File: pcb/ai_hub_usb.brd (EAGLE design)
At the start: 82.5 x 38.1 mm, 31 parts, among them IC1 FE1.1S

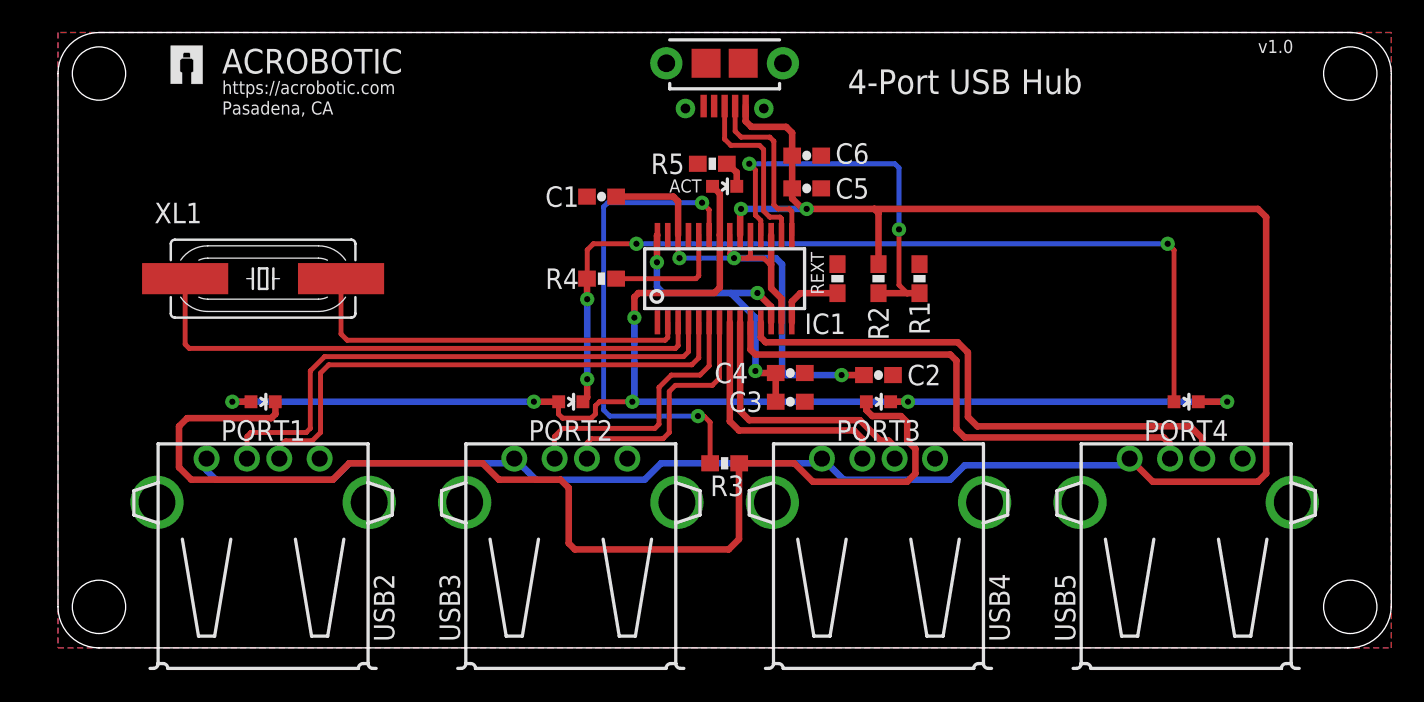
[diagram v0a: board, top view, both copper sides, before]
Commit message: redesign: gang power control, smaller layout
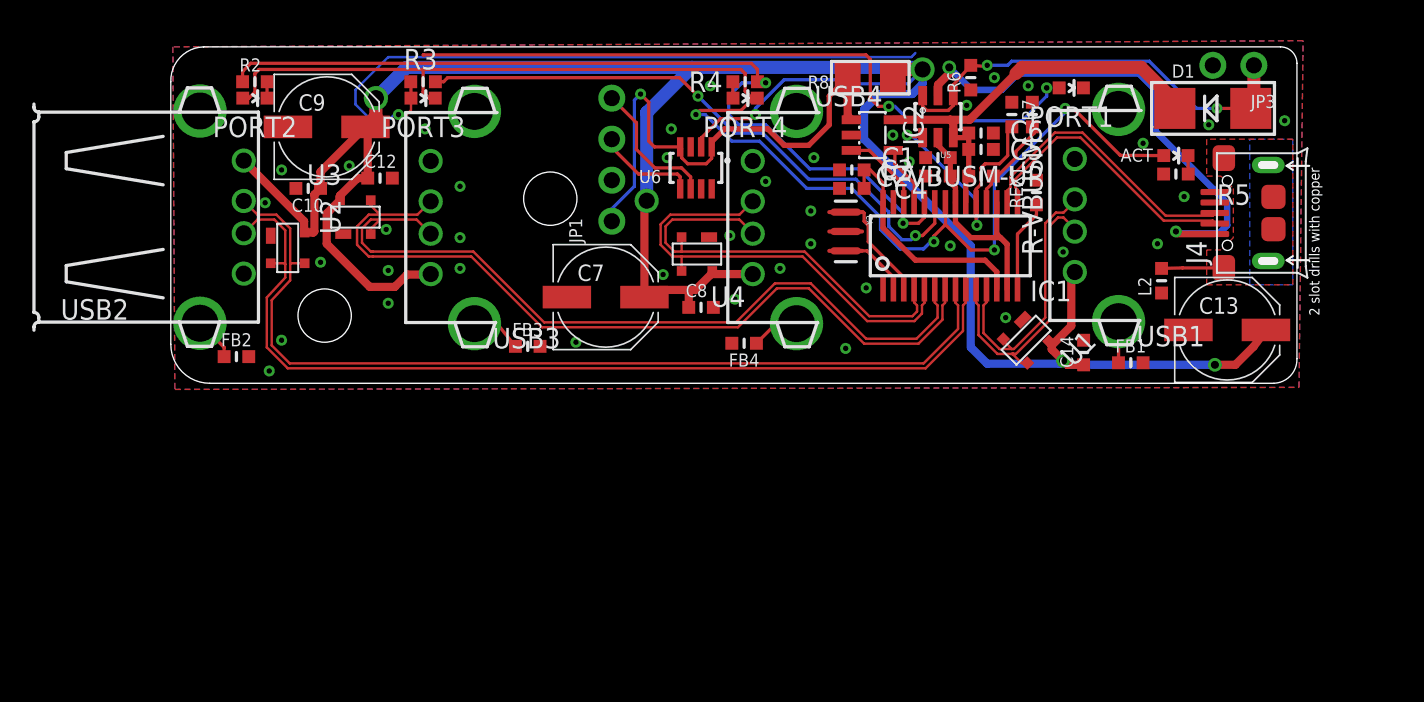
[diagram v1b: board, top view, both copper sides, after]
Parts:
- removed FRAME1: FRAME-LETTER, Ai_Miscellany:CREATIVE-COMMONS
- removed R1: 100K, Ai_Passives:RES-0603
- removed STANDOFF2, STANDOFF3: STAND-OFF4, Ai_Electromechanical:STAND-OFF-4
- removed U$5, U$6: AI-LOGOXS, Ai_Miscellany:AI-LOGO-XS
- removed USB5: USBA-PTH, Ai_Connectors:USB-A-F-PTH
- removed XL1: 12MHz, Ai_FrequencyControl:HC49UP
- added C10, C12, C14, C8: 0.1uF, microbuilder:_0603MP
- added C13, C7, C9: (no value), SparkFun-Passives:PANASONIC_D
- added D1: (no value), microbuilder:SMADIODE
- added FB1, FB2, FB3, FB4, L2: (no value), microbuilder:_0603MP
- added IC2: TPS2041BDBV, tps204xb_205xb:SOT23-5L
- added J4: MICRO-B-SMD_340005001, connectors:MICRO-USB
- added JP1: (no value), microbuilder:1X04_ROUND
- added JP3: (no value), microbuilder:1X02_ROUND
- added R-VBUSM, R6, R7: 100K, microbuilder:_0603MP
- added R-VBUSM-UP: 47K, microbuilder:_0603MP
- added R8: (no value), microbuilder:1206
- added U1, U2, U3, U4: PRTR5V0U2X, esd:SOT-143B
- added U5: IRF5810TRPBF, SparkFun-DiscreteSemi:SOT23-6
- added U6: (no value), microbuilder:SOT23-8
- added Y2: 12MHZ, SparkFun-FreqCtrl:RESONATOR-SMD
- C1, C2, C3, C4, C5, C6: device Ai_Passives:CAP-0603 -> microbuilder:_0603MP
- R2: value 47K -> 330; device Ai_Passives:RES-0603 -> microbuilder:_0603MP
- R3, R4, R5, REXT: device Ai_Passives:RES-0603 -> microbuilder:_0603MP
- USB1: value USBMICROB-PTH -> USBA-PTH-VERTICAL; device Ai_Connectors:USB-MICROB-TH -> ai_hub_usb:USB-A-F-PTH-VERTICAL
- USB2: device Ai_Connectors:USB-A-F-PTH -> ai_hub_usb:USB-A-F-PTH
- USB3, USB4: value USBA-PTH -> USBA-PTH-VERTICAL; device Ai_Connectors:USB-A-F-PTH -> ai_hub_usb:USB-A-F-PTH-VERTICAL
- moved PORT1 53.7 mm to (62.7, 34.7)
- moved STANDOFF4 50.1 mm to (30.5, 27.8)
- moved R2 40.5 mm to (12.2, 35.1), turned to 0 degrees
- moved PORT3 33.9 mm to (22.6, 34.0)
- moved PORT4 33.1 mm to (42.5, 34.0)
- moved R3 30.1 mm to (22.6, 35.1), turned to 180 degrees
- moved R5 28.7 mm to (69.2, 29.3)
- moved ACT 28.0 mm to (69.2, 30.5)
- moved PORT2 27.1 mm to (12.2, 34.0)
- moved USB1 25.5 mm to (65.0, 26.8), turned to 90 degrees
- moved USB3 21.4 mm to (25.1, 26.7), turned to 90 degrees
- moved USB2 21.4 mm to (6.13, 26.7), turned to 270 degrees
- moved USB4 21.1 mm to (45.1, 26.7), turned to 90 degrees
- moved C1 21.0 mm to (54.5, 30.4)
- moved STANDOFF1 20.5 mm to (16.5, 20.6)
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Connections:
- net N$23 renamed LED1
- net N$25 renamed DRV
- net N$8 renamed VCC1V8
- removed net 3V3: C1.1, C2.1, IC1.13, IC1.17, IC1.19, IC1.21, IC1.26
- removed net N$11: IC1.11, USB5.D+
- removed net N$12: IC1.10, USB5.D-
- removed net N$13: IC1.18, R1.2, R2.1
- removed net N$14: IC1.9, USB4.D+
- removed net N$15: IC1.8, USB4.D-
- removed net N$16: IC1.7, USB3.D+
- removed net N$17: IC1.6, USB3.D-
- removed net N$18: IC1.5, USB2.D+
- removed net N$19: IC1.4, USB2.D-
- removed net N$24: IC1.24, R4.1
- removed net N$9: IC1.3, XL1.1
- new net BUSJ: IC1.19, R7.2, U5.6
- new net LED2: IC1.24, R2.1, R4.1
- new net N$4: FB3.1, USB3.SHIELD@1, USB3.SHIELD@2
- new net N$5: FB4.1, USB4.SHIELD@1, USB4.SHIELD@2
- new net OSC_IN: IC1.3, Y2.1
- new net OSC_OUT: IC1.2, Y2.3
- new net OVRCUR: IC1.26, IC2.3
- new net PWREN: IC1.25, IC2.4
- new net SCL: JP1.3, U6.5
- new net SDA: JP1.4, U6.6
- new net TEST: IC1.27
- new net USB1_D_N: IC1.10, U1.3, USB1.D-
- new net USB1_D_P: IC1.11, U1.2, USB1.D+
- new net USB2_D_N: IC1.8, U2.3, USB2.D-
- new net USB2_D_P: IC1.9, U2.2, USB2.D+
- new net USB3_D_N: IC1.6, U3.2, USB3.D-
- new net USB3_D_P: IC1.7, U3.3, USB3.D+
- new net USB4_D_N: IC1.4, U4.2, USB4.D-
- new net USB4_D_P: IC1.5, U4.3, USB4.D+
- new net USB_D_N: IC1.15, J4.2
- new net USB_D_P: IC1.16, J4.3
- new net USB_SHIELD: J4.S1, J4.S2, J4.S3, J4.S4, J4.S5, J4.S6, L2.2
- new net VBUS_MANAGED: C10.1, C12.1, C13.+, C14.1, C7.+, C8.1, C9.+, R8.1, U1.4, U2.4, U3.4, U4.4, U6.2, USB1.VBUS, USB2.VBUS, USB3.VBUS, USB4.VBUS
- new net VBUS_MONITOR: IC1.18, R-VBUSM-UP.1, R-VBUSM.2
- new net VBUS_SENSE: IC2.1, JP1.1, R8.2, U6.1, U6.4
- new net VBUS_UPSTREAM: J4.1, U5.2
- new net VCC3V3: C1.1, C2.1, IC1.13, IC1.17, IC1.21, U5.5
- new net VEXT: D1.A, JP3.1, R6.2, U5.1, U5.3
- net GND: now also C10.2, C12.2, C13.-, C14.2, C7.-, C8.2, C9.-, FB1.2, FB2.2, FB3.2, FB4.2, IC2.2, J4.5, JP1.2, JP3.2, L2.1, R-VBUSM.1, R6.1, R7.1, U1.1, U2.1, U3.1, U4.1, U6.3, U6.7, U6.8, Y2.2; no longer R1.1, USB5.GND
- net N$2: now also FB1.1, USB1.SHIELD@1, USB1.SHIELD@2; no longer IC1.15, USB1.D-
- net N$3: now also FB2.1, USB2.SHIELD@1, USB2.SHIELD@2; no longer IC1.16, USB1.D+
- net N$6: now also R2.2; no longer PORT4.A, R4.2
- net N$7: now also PORT4.A, R4.2; no longer IC1.2, XL1.2
- net VBUS: now also D1.C, IC2.5, R-VBUSM-UP.2, U5.4; no longer R2.2, USB1.VBUS, USB2.VBUS, USB3.VBUS, USB4.VBUS, USB5.VBUS
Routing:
- net VBUS_MANAGED: track 0.00 -> 161.2 mm, vias 0 -> 6
- net VBUS: track 133.2 -> 26.8 mm, vias 2 -> 0
- net USB2_D_P: track 0.00 -> 59.1 mm
- net USB2_D_N: track 0.00 -> 58.5 mm
- net N$6: track 55.6 -> 1.02 mm, vias 4 -> 0
- net LED2: track 0.00 -> 54.3 mm, vias 0 -> 2
- net USB3_D_P: track 0.00 -> 50.8 mm
- net USB3_D_N: track 0.00 -> 49.3 mm
- net 3V3: track 37.0 -> 0.00 mm, vias 3 -> 0
- net N$9: track 36.2 -> 0.00 mm
- net N$19: track 34.8 -> 0.00 mm
- net N$11: track 34.4 -> 0.00 mm
- net N$12: track 33.5 -> 0.00 mm
- net N$18: track 33.3 -> 0.00 mm
- net VBUS_SENSE: track 0.00 -> 33.2 mm, vias 0 -> 1
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- added copper zone on layer 1, net USB_SHIELD
- added copper zone on layer 16, net USB_SHIELD
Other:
- board size 82.5 x 38.1 mm -> 69.7 x 20.8 mm
- board text removed: "4-Port USB Hub"
- board text removed: "@MakerBro"
- board text removed: "ACROBOTIC"
- board text removed: "Pasadena, CA"
- board text removed: "https://acrobotic.com"
- board text removed: "v1.0"
